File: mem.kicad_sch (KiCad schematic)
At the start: 4 parts, among them SW83 SW_Push, U3 W25Q128JVS

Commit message: adding labels and updating PCB
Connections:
- net QSPI_SS: now reaches R1.1, U3.1 (~{CS})
- net QSPI_SD1: now reaches U3.2 (DO/IO_{1})
- net QSPI_SD2: now reaches U3.3 (~{WP}/IO_{2})
- net QSPI_SD0: now reaches U3.5 (DI/IO_{0})
- net QSPI_SCLK: now reaches U3.6 (CLK)
- net QSPI_SD3: now reaches U3.7 (~{HOLD}/~{RESET}/IO_{3})
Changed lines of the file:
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@@
+	(wire
+		(pts
+			(xy 144.78 77.47) (xy 148.59 77.47)
+		)
+		(stroke
+			(width 0)
+			(type default)
+		)
+	)
 	(wire
 		(pts
@@
 		(pts
 			(xy 158.75 54.61) (xy 166.37 54.61)
+		)
+		(stroke
+			(width 0)
+			(type default)
+		)
+	)
+	(wire
+		(pts
+			(xy 144.78 82.55) (xy 148.59 82.55)
+		)
+		(stroke
+			(width 0)
+			(type default)
+		)
+	)
+	(wire
+		(pts
+			(xy 144.78 85.09) (xy 148.59 85.09)
+		)
+		(stroke
+			(width 0)
+			(type default)
+		)
+	)
+	(wire
+		(pts
+			(xy 144.78 74.93) (xy 148.59 74.93)
 		)
 		(stroke
@@
 		)
 	)
+	(wire
+		(pts
+			(xy 144.78 80.01) (xy 148.59 80.01)
+		)
+		(stroke
+			(width 0)
+			(type default)
+		)
+	)
+	(label "QSPI_SS"
+		(at 148.59 72.39 180)
+		(effects
+			(font
+				(size 1.27 1.27)
+			)
+			(justify right bottom)
+		)
+	)
+	(label "QSPI_SD1"
+		(at 148.59 80.01 180)
+		(effects
+			(font
+				(size 1.27 1.27)
+			)
+			(justify right bottom)
+		)
+	)
+	(label "QSPI_SD3"
+		(at 148.59 85.09 180)
+		(effects
+			(font
+				(size 1.27 1.27)
+			)
+			(justify right bottom)
+		)
+	)
+	(label "QSPI_SD2"
+		(at 148.59 82.55 180)
+		(effects
+			(font
+				(size 1.27 1.27)
+			)
+			(justify right bottom)
+		)
+	)
+	(label "QSPI_SCLK"
+		(at 148.59 74.93 180)
+		(effects
+			(font
+				(size 1.27 1.27)
+			)
+			(justify right bottom)
+		)
+	)
+	(label "QSPI_SD0"
+		(at 148.59 77.47 180)
+		(effects
+			(font
+				(size 1.27 1.27)
+			)
+			(justify right bottom)
+		)
+	)

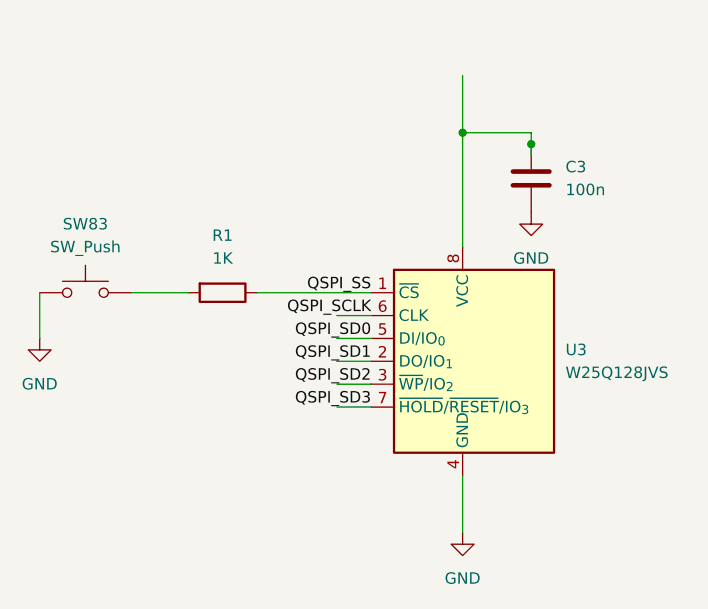
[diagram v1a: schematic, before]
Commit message: Added potentially better Japanese Duplex Matrix
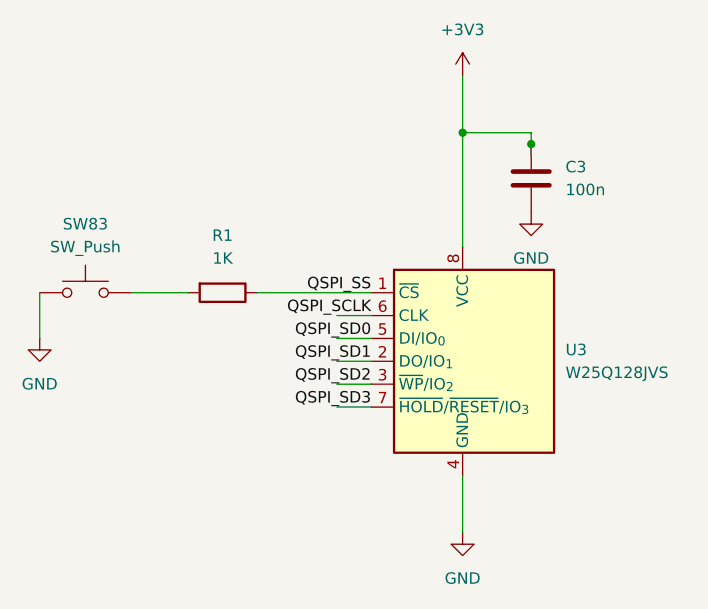
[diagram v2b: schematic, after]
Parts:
- SW83: footprint (none) -> Button_Switch_SMD:SW_Push_1P1T_NO_E-Switch_TL3301NxxxxxG
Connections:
- net +3V3: now reaches C3.1, U3.8 (VCC)
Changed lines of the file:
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@@
 			)
 		)
-		(property "Footprint" ""
+		(property "Footprint" "Button_Switch_SMD:SW_Push_1P1T_NO_E-Switch_TL3301NxxxxxG"
 			(at 116.84 67.31 0)
 			(effects
@@
 					(unit 1)
 				)
+			)
+		)
+	)
+	(symbol
+		(lib_id "power:+3V3")
+		(at 158.75 48.26 0)
+		(unit 1)
+		(exclude_from_sim no)
+		(in_bom yes)
+		(on_board yes)
+		(dnp no)
+		(fields_autoplaced yes)
+		(property "Reference" "#PWR013"
+			(at 158.75 52.07 0)
+			(effects
+				(font
+					(size 1.27 1.27)
+				)
+				(hide yes)
+			)
+		)
+		(property "Value" "+3V3"
+			(at 158.75 43.18 0)
+			(effects
+				(font
+					(size 1.27 1.27)
+				)
+			)
+		)
+		(property "Footprint" ""
+			(at 158.75 48.26 0)
+			(effects
+				(font
+					(size 1.27 1.27)
+				)
+				(hide yes)
+			)
+		)
+		(property "Datasheet" ""
+			(at 158.75 48.26 0)
+			(effects
+				(font
+					(size 1.27 1.27)
+				)
+				(hide yes)
+			)
+		)
+		(property "Description" "Power symbol creates a global label with name \"+3V3\""
+			(at 158.75 48.26 0)
+			(effects
+				(font
+					(size 1.27 1.27)
+				)
+				(hide yes)
+			)
+		)
+		(pin "1"
+		)
+		(instances
+			(project ""
+				(path "/75d7688f-df99-426a-b593-390936606183/572b8eec-91ac-4047-ae36-918ae2dd5ec4/176b07a5-e53c-4150-8ae3-822bba4cc850"
+					(reference "#PWR013")
+					(unit 1)
+				)
